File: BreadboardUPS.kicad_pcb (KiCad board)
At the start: 2 copper layers, 111 parts, among them J101 Output1, J102 Output1, J103 Output1, J104 Ctrl, J105 Output2, J106 Output2, J107 Output2, J202 USBC, J203 DC In, Q401 DO2308S, Q402 DO2309A, Q403 DO2309A, Q501 DO2308S, Q502 DO2309A, Q503 DO2309A, SW401 Vsel, SW402 PWR_ON, SW501 Vsel, SW502 PWR_ON, U201 TPS630701RNMR, U301 BQ24090DGQ, U302 BQ27441-G1, U401 TPS630701RNMR, U501 TPS630701RNMR

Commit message: PCB layout
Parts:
- removed C501, C506, C507: 10u, Capacitor_SMD:C_1206_3216Metric_Pad1.33x1.80mm_HandSolder
- removed C502, C504: 100n, Capacitor_SMD:C_1206_3216Metric_Pad1.33x1.80mm_HandSolder
- removed C503: 1u, Capacitor_SMD:C_0805_2012Metric_Pad1.18x1.45mm_HandSolder
- removed C505: 10u, Capacitor_Tantalum_SMD:CP_EIA-7343-31_Kemet-D_HandSolder
- removed D501: PWR, LED_SMD:LED_1206_3216Metric_Pad1.42x1.75mm_HandSolder
- removed J102, J103: Output1, Connector_PinHeader_2.54mm:PinHeader_1x02_P2.54mm_Vertical
- removed J105, J106, J107: Output2, Connector_PinHeader_2.54mm:PinHeader_1x02_P2.54mm_Vertical
- removed JP101: Single/Dual Supply, Jumper:SolderJumper-3_P1.3mm_Open_RoundedPad1.0x1.5mm
- removed L501: 1.5u, Inductor_SMD:L_Cenker_CKCS4020
- removed Q501: DO2308S, Package_TO_SOT_SMD:SOT-23_Handsoldering
- removed Q502, Q503: DO2309A, Package_TO_SOT_SMD:SOT-23_Handsoldering
- removed R501, R502, R503, R504, R508: 10k, Resistor_SMD:R_1206_3216Metric_Pad1.30x1.75mm_HandSolder
- removed R505: 220k, Resistor_SMD:R_0805_2012Metric_Pad1.20x1.40mm_HandSolder
- removed R506: 470k, Resistor_SMD:R_0805_2012Metric_Pad1.20x1.40mm_HandSolder
- removed R507: 150k, Resistor_SMD:R_0805_2012Metric_Pad1.20x1.40mm_HandSolder
- removed R509: 220, Resistor_SMD:R_1206_3216Metric_Pad1.30x1.75mm_HandSolder
- removed SW501: Vsel, Button_Switch_THT:SW_Slide_SPDT_Straight_CK_OS102011MS2Q
- removed SW502: PWR_ON, Button_Switch_THT:SW_PUSH_6mm
- removed TP501: VSEL, TestPoint:TestPoint_Pad_D2.0mm
- removed TP502: EN, TestPoint:TestPoint_Pad_D2.0mm
- removed TP503: ~{PG}, TestPoint:TestPoint_Pad_D2.0mm
- removed TP504: VCC, TestPoint:TestPoint_Pad_D2.0mm
- removed U501: TPS630701RNMR, lib:TPS63070
- C201, C202, C203, C205, C206, C207, C301, C302, C303, C304, C401, C402, C403, C404, C405, C406, C407, D202, D303, D304, L201, L401, Q401, Q402, Q403, R303, R306, R307, R401, R402, R403, R404, R405, R406, R407, R408, R409, TP201, TP202, TP301, TP302, TP303, TP401, TP402, TP403, TP404, U201, U301, U302, U401: moved to B.Cu
- J101: value Output1 -> Output; footprint Connector_PinHeader_2.54mm:PinHeader_1x02_P2.54mm_Vertical -> Connector_PinHeader_2.54mm:PinHeader_2x05_P2.54mm_Vertical; moved to B.Cu
- moved BT301 151.6 mm to (148.0, 75.5), turned to -90 degrees
- moved J101 151.0 mm to (122.2, 84.8)
- moved SW402 141.0 mm to (124.8, 113.8), turned to 90 degrees
- moved TP402 135.8 mm to (127.0, 118.0), turned to 180 degrees
- moved TP201 130.4 mm to (155.8, 148.5), turned to 180 degrees
- moved SW401 128.9 mm to (134.0, 112.2), turned to 90 degrees
- moved C203 128.8 mm to (143.5, 149.5), turned to 180 degrees
- moved C201 128.6 mm to (143.5, 151.8), turned to 180 degrees
- moved L201 126.5 mm to (148.5, 144.0), turned to 90 degrees
- moved TP401 125.0 mm to (130.5, 98.5), turned to 180 degrees
- moved J203 124.8 mm to (134.0, 144.8)
- moved C301 124.6 mm to (155.9, 107.5)
- moved C202 123.7 mm to (143.5, 147.2), turned to 180 degrees
- moved U401 123.2 mm to (144.2, 89.0)
- moved TP404 123.2 mm to (123.8, 89.8), turned to 180 degrees
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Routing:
- net /Charging/Vout: track 0.00 -> 76.2 mm, vias 0 -> 4
- net /Supply1/EN: track 0.00 -> 67.1 mm, vias 0 -> 2
- net Net-(BT301-+): track 0.00 -> 47.8 mm, vias 0 -> 3
- net /Charging/Vin: track 0.00 -> 45.5 mm, vias 0 -> 12
- net Net-(D202-A): track 0.00 -> 39.8 mm, vias 0 -> 2
- net /Supply1/VSEL: track 0.00 -> 34.6 mm, vias 0 -> 1
- net /PWR_CTRL: track 0.00 -> 31.7 mm, vias 0 -> 1
- net /SDA: track 0.00 -> 28.6 mm, vias 0 -> 1
- net /SCL: track 0.00 -> 26.3 mm, vias 0 -> 1
- net /BAT_LOW: track 0.00 -> 25.8 mm, vias 0 -> 4
- net /Supply1/Vout: track 0.00 -> 25.3 mm, vias 0 -> 11
- net Net-(D401-A): track 0.00 -> 24.1 mm, vias 0 -> 1
- net Net-(U301-~{PG}): track 0.00 -> 20.1 mm, vias 0 -> 2
- net /Charging/VBAT: track 0.00 -> 18.1 mm, vias 0 -> 9
- net Net-(U201-PG): track 0.00 -> 18.0 mm, vias 0 -> 2
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- added copper zone on B.Cu, net /Charging/VBAT
- added copper zone on F.Cu, net /Charging/VBAT
- added copper zone on B.Cu, net /Charging/Vin
- added copper zone on F.Cu, net /Charging/Vin
- added copper zone on F.Cu, net /Supply1/Vout
- added copper zone on B.Cu, net GND
- added copper zone on B.Cu, net Net-(BT301-+)
- added copper zone on F.Cu, net Net-(C201-Pad1)
- added copper zone on B.Cu, net Net-(U201-L1)
- added copper zone on B.Cu, net Net-(U201-L2)
- added copper zone on B.Cu, net Net-(U401-L1)
- added copper zone on B.Cu, net Net-(U401-L2)
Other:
- board outline added: 39.2 x 81 mm

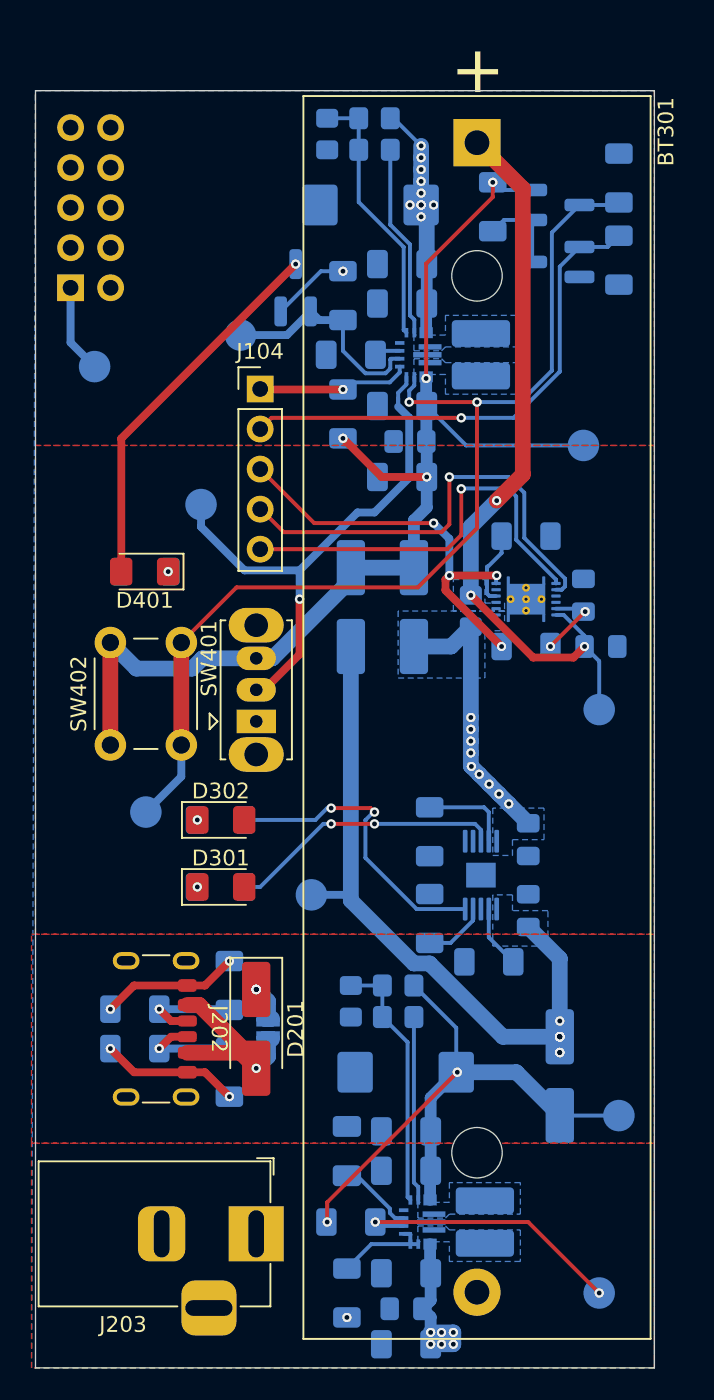
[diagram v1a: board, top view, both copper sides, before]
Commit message: Text and silk mask for manufacturing
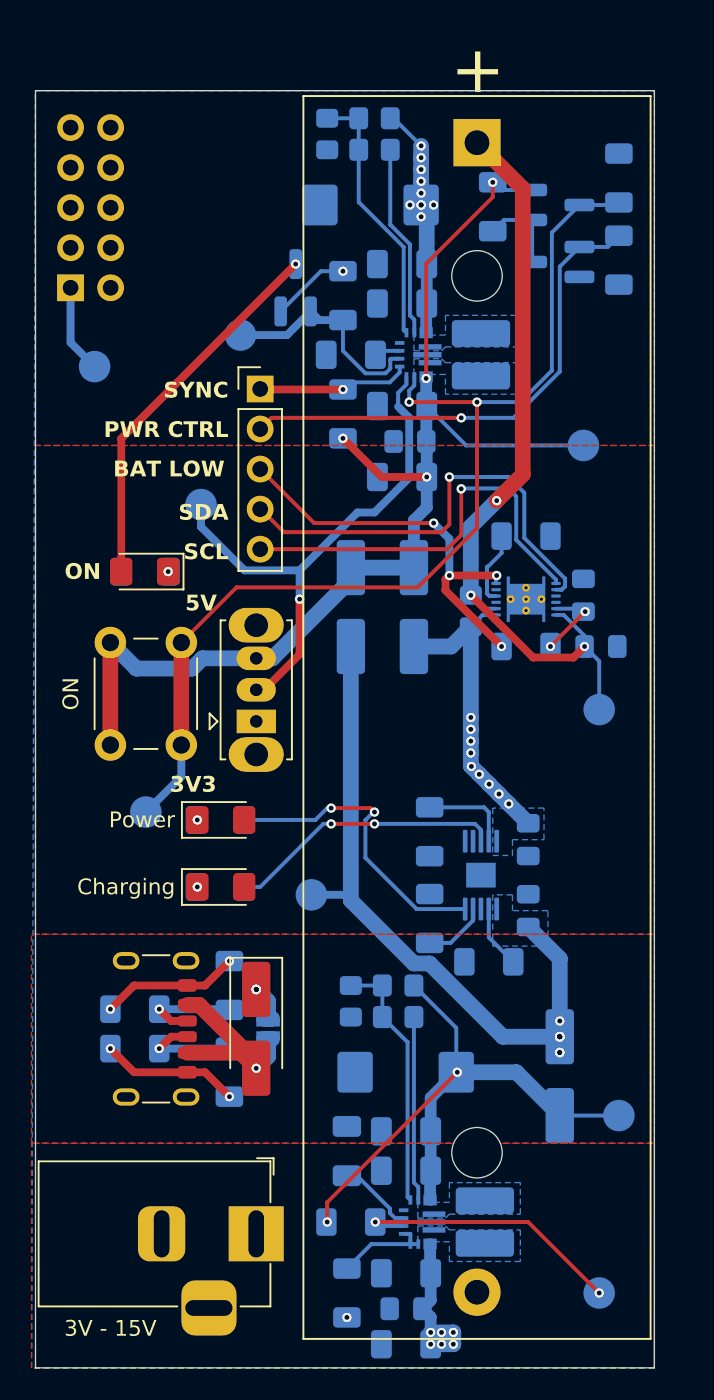
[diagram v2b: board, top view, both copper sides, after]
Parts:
- D302: value ExternalPower -> Power
- D401: value PWR -> ON
- J203: value DC In -> 3V - 15V
- SW402: value PWR_ON -> ON
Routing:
- net Net-(BT301-+): track 47.8 -> 49.8 mm
- net /Charging/VBAT: track 18.1 -> 20.0 mm
- removed copper zone on B.Cu, net Net-(BT301-+)
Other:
- board text added: "3V3"
- board text added: "5V"
- board text added: "BAT LOW"
- board text added: "PWR CTRL"
- board text added: "SCL"
- board text added: "SDA"
- board text added: "SYNC"

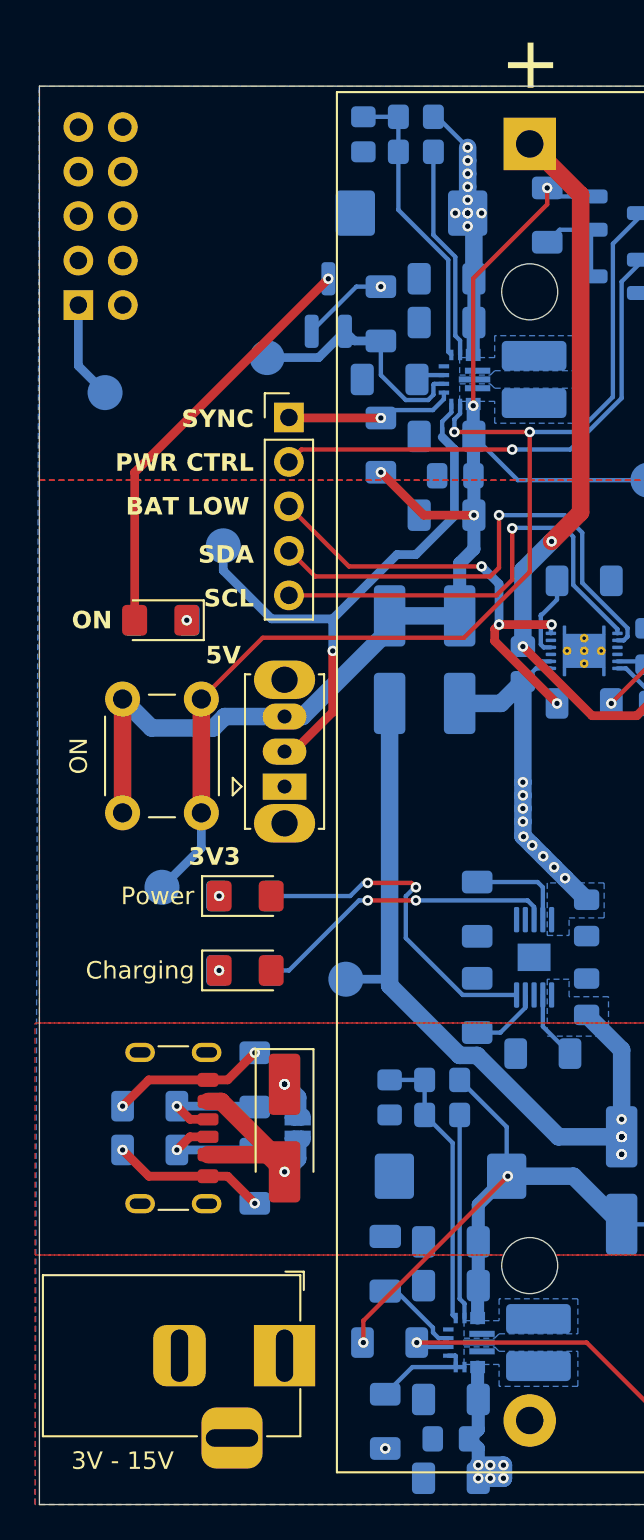
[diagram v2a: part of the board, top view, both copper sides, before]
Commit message: Add external battery connector
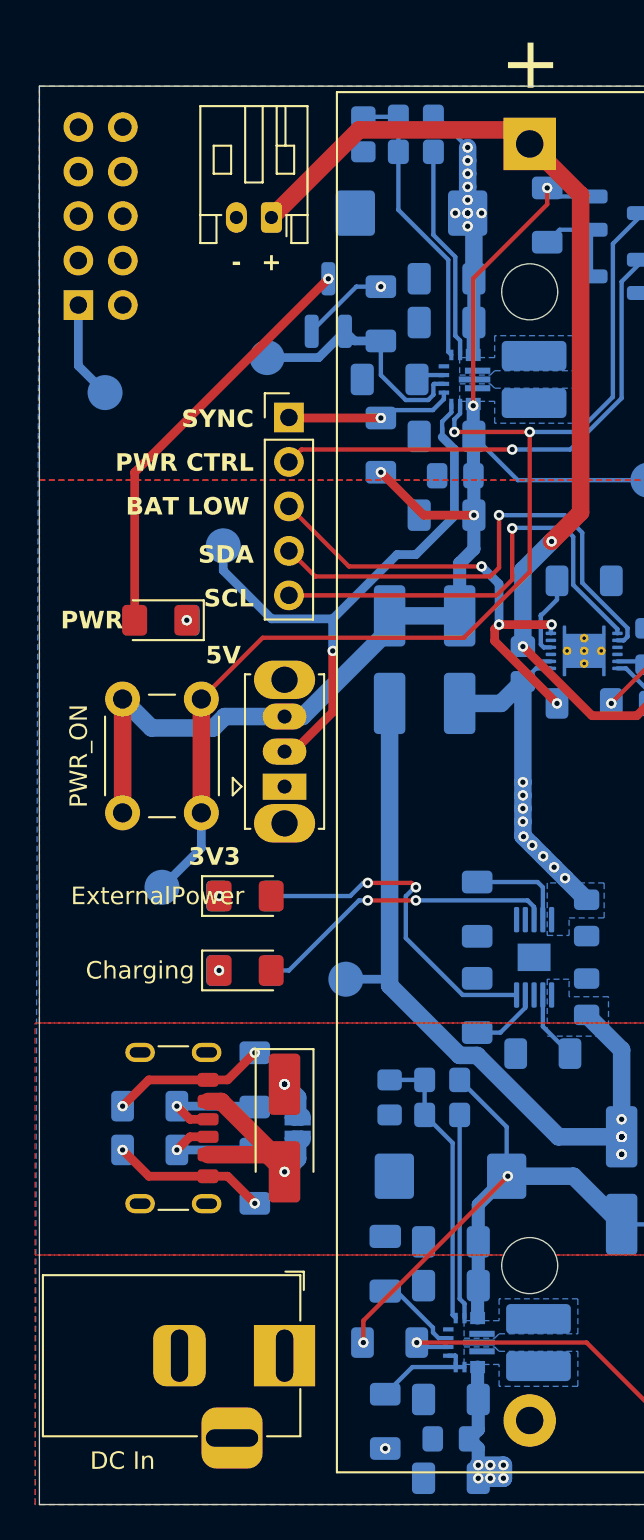
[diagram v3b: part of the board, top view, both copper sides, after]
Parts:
- added J301: BAT, Connector_JST:JST_PH_S2B-PH-K_1x02_P2.00mm_Horizontal, F.Cu at (133.2, 79.8)
- D302: value Power -> ExternalPower
- D401: value ON -> PWR
- J203: value 3V - 15V -> DC In
- SW402: value ON -> PWR_ON
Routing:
- net Net-(BT301-+): track 49.8 -> 66.9 mm
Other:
- board text added: "+"
- board text added: "-"

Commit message: Address DRC warnings and errors
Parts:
- D301: value Charging -> Chrg
- D302: value ExternalPower -> ExtPwr
- moved D201 2.44 mm to (131.6, 131.8)
- moved JP201 2.44 mm to (132.3, 131.8)
- moved R203 2.44 mm to (129.9, 134.5)
- moved R207 2.44 mm to (129.9, 129.0)
- moved J202 2.44 mm to (124.1, 131.8)
- moved R202 2.44 mm to (123.9, 133.0)
- moved R208 2.44 mm to (123.9, 130.5)
- moved J203 0.62 mm to (134.6, 144.8)
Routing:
- net /Supply1/VSEL: track 34.6 -> 34.1 mm
- net /Supply1/Vout: vias 11 -> 10
- net /Charging/Vin: vias 12 -> 8

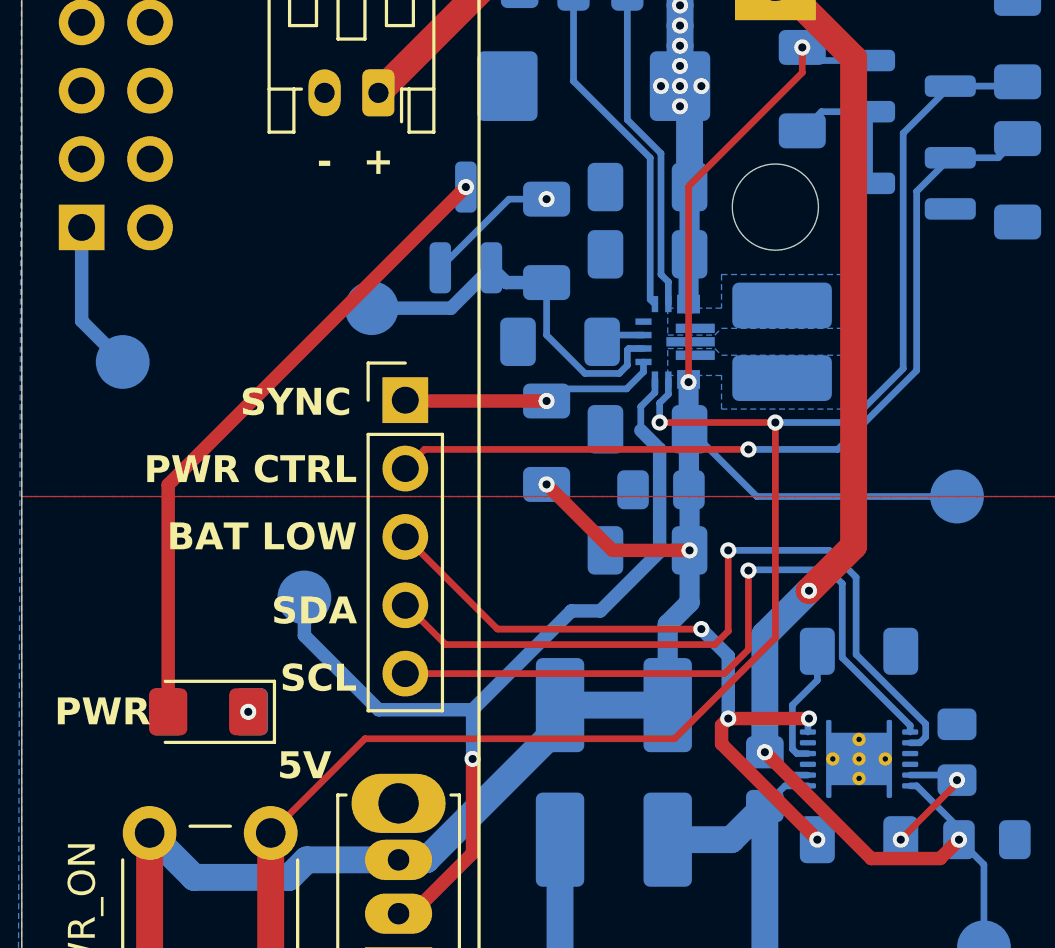
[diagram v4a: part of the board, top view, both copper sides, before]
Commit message: Resolve DRC issues
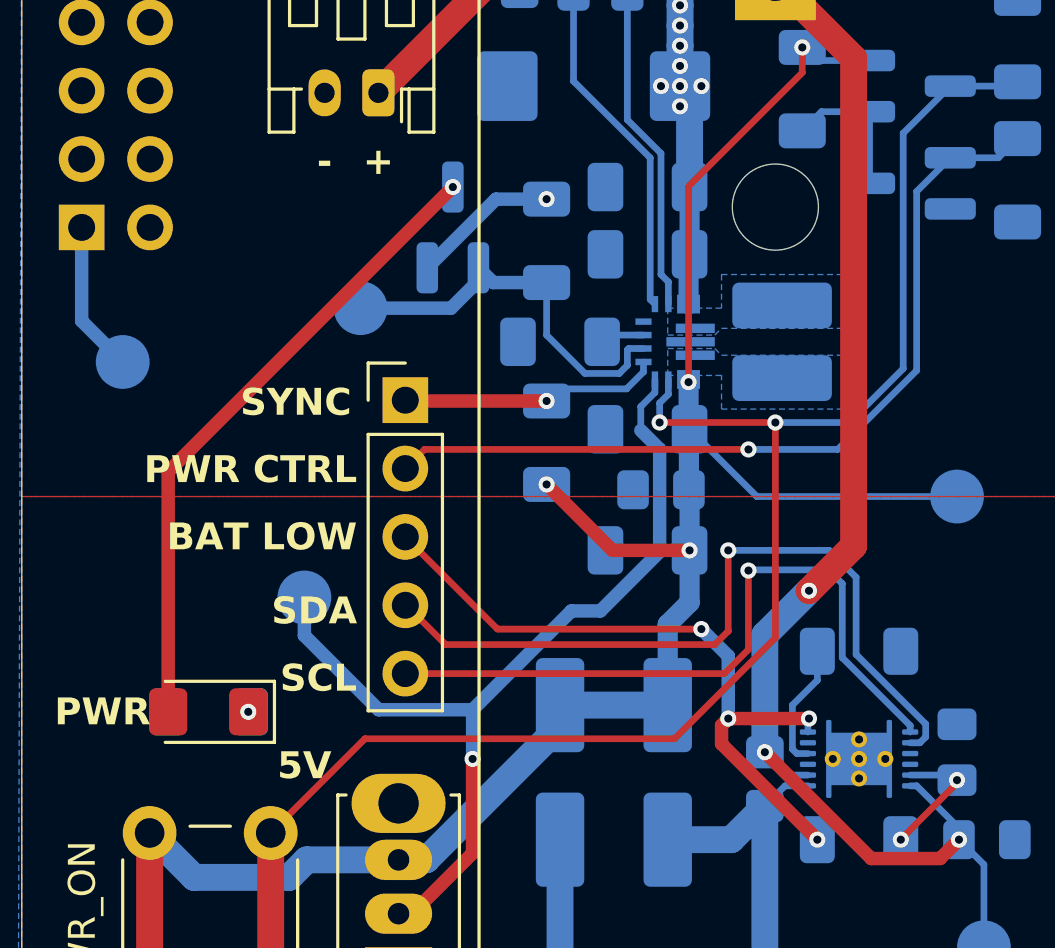
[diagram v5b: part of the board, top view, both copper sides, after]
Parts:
- moved Q403 0.48 mm to (136.0, 84.8)
- moved TP403 0.41 mm to (132.6, 87.8)
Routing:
- net Net-(Q403-G): track 14.2 -> 14.9 mm
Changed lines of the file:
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@@
 		(pad "13" thru_hole circle
 			(at -0.975 0 180)
-			(size 0.5 0.5)
-			(drill 0.2)
+			(size 0.6 0.6)
+			(drill 0.3)
 			(property pad_prop_heatsink)
 			(layers "*.Cu")
@@
 		(pad "13" thru_hole circle
 			(at 0 -0.725 180)
-			(size 0.5 0.5)
-			(drill 0.2)
+			(size 0.6 0.6)
+			(drill 0.3)
 			(property pad_prop_heatsink)
 			(layers "*.Cu")
@@
 		(pad "13" thru_hole circle
 			(at 0 0 180)
-			(size 0.5 0.5)
-			(drill 0.2)
+			(size 0.6 0.6)
+			(drill 0.3)
 			(property pad_prop_heatsink)
 			(layers "*.Cu")
@@
 		(pad "13" thru_hole circle
 			(at 0 0.725 180)
-			(size 0.5 0.5)
-			(drill 0.2)
+			(size 0.6 0.6)
+			(drill 0.3)
 			(property pad_prop_heatsink)
 			(layers "*.Cu")
@@
 		(pad "13" thru_hole circle
 			(at 0.975 0 180)
-			(size 0.5 0.5)
-			(drill 0.2)
+			(size 0.6 0.6)
+			(drill 0.3)
 			(property pad_prop_heatsink)
 			(layers "*.Cu")
@@
 	(footprint "Package_TO_SOT_SMD:SOT-23_Handsoldering"
 		(layer "B.Cu")
-		(at 136.5 84.75 90)
+		(at 136.017 84.75 90)
 		(descr "SOT-23, Handsoldering")
 		(tags "SOT-23")
@@
 	(footprint "TestPoint:TestPoint_Pad_D2.0mm"
 		(layer "B.Cu")
-		(at 133 87.75 180)
+		(at 132.588 87.75 180)
 		(descr "SMD pad as test Point, diameter 2.0mm")
 		(tags "test point SMD pad")
@@
 	)
 	(segment
-		(start 135.55 86.25)
-		(end 138.1 83.7)
-		(width 0.25)
+		(start 137.617 83.7)
+		(end 139.5 83.7)
+		(width 0.5)
 		(layer "B.Cu")
 		(net 11)
@@
 	)
 	(segment
-		(start 138.1 83.7)
-		(end 139.5 83.7)
-		(width 0.25)
-		(layer "B.Cu")
-		(net 11)
-	)
-	(segment
 		(start 122.225 88.225)
 		(end 122.225 84.83)
@@
 	)
 	(segment
+		(start 135.067 86.25)
+		(end 137.617 83.7)
+		(width 0.5)
+		(layer "B.Cu")
+		(net 11)
+	)
+	(segment
 		(start 144.4575 79.5)
 		(end 144.4575 78)
@@
 	)
 	(segment
-		(start 125.44 102.75)
-		(end 125.44 94.31)
+		(start 125.44 93.827)
+		(end 125.44 102.75)
 		(width 0.5)
 		(layer "F.Cu")
@@
 	)
 	(segment
-		(start 125.44 94.31)
-		(end 136.5 83.25)
+		(start 136.017 83.25)
+		(end 125.44 93.827)
 		(width 0.5)
 		(layer "F.Cu")
@@
 	)
 	(via
-		(at 136.5 83.25)
+		(at 136.017 83.25)
 		(size 0.6)
 		(drill 0.3)
@@
 	)
 	(segment
-		(start 135.95 87.75)
-		(end 137.45 86.25)
-		(width 0.5)
-		(layer "B.Cu")
-		(net 35)
-	)
-	(segment
 		(start 140.925196 90.176)
 		(end 139.5 88.750804)
@@
 	)
 	(segment
-		(start 133 87.75)
+		(start 132.588 87.75)
 		(end 135.95 87.75)
 		(width 0.5)
@@
 	)
 	(segment
-		(start 139.5 86.8)
-		(end 138 86.8)
+		(start 137.517 86.8)
+		(end 139.5 86.8)
+		(width 0.5)
+		(layer "B.Cu")
+		(net 35)
+	)
+	(segment
+		(start 135.95 87.75)
+		(end 136.967 86.733)
 		(width 0.5)
 		(layer "B.Cu")
@@
 	)
 	(segment
-		(start 138 86.8)
-		(end 137.45 86.25)
-		(width 0.5)
+		(start 142.550001 89.250002)
+		(end 142.501 89.299003)
+		(width 0.25)
 		(layer "B.Cu")
 		(net 35)
 	)
 	(segment
-		(start 142.550001 89.250002)
-		(end 142.501 89.299003)
-		(width 0.25)
+		(start 136.967 86.25)
+		(end 137.517 86.8)
+		(width 0.5)
 		(layer "B.Cu")
 		(net 35)
@@
 		(layer "B.Cu")
 		(net 35)
+	)
+	(segment
+		(start 136.967 86.733)
+		(end 136.967 86.25)
+		(width 0.5)
+		(layer "B.Cu")
+		(net 35)
